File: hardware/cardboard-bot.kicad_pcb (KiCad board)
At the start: 2 copper layers, 80 x 46 mm, 101 parts, among them J1 USB-C CHARGE, J10 ESC PWR 2, J2 I2C, J3 MOTOR L, J4 MOTOR R, J5 OUT1, J6 OUT2, J7 IO3, J8 IO21, J9 ESC PWR 1, Q1 CJAC80N03 DSG, Q2 CJAC80N03 CHG, Q3 AGM30P05A, SW1 POWER, U1 BQ25887RGER, U2 HY2120-CB, U3 TPS563201DDCR, U4 XIAO ESP32-C3, U5 DRV8833PWPR, U6 74VHCT1G125

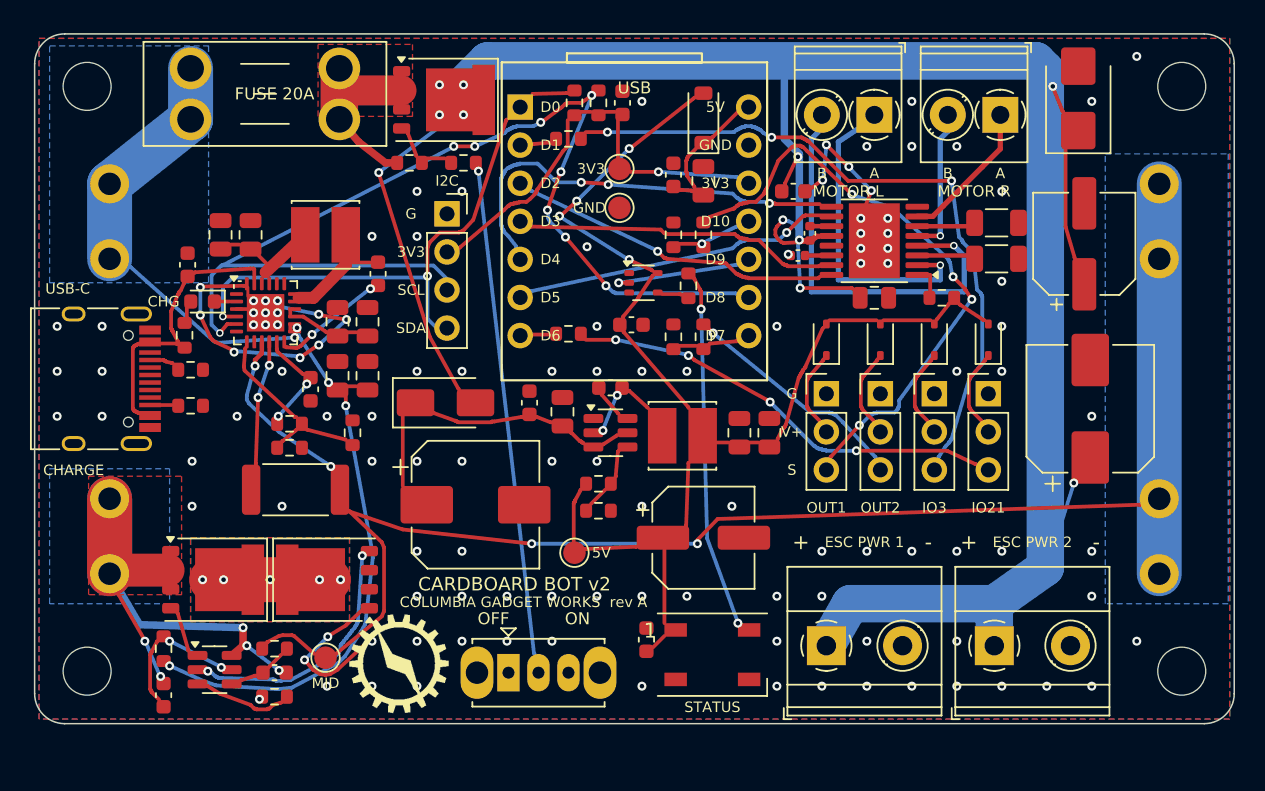
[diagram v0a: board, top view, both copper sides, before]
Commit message: Rework BOM for JLC stock: IP2320 charger, Basic parts, no shortfalls
Swap every out-of-stock or short part for a Basic, no-fee Preferred, or high-stock Extended part
(stock checked 28 Oct 2026):

- Charger: BQ25887 -> IP2320 (8.40 V / 1.0 A straps), plus 2x HY2213-BB3A cell balancers
  with AO3401A + 100R bleed
- Buck: TPS563201 (out of stock) -> TPS54202, same SOT-23-6 pinout, 75k/10k feedback
- Status LED: WS2812B-B (out of stock) -> XL-5050RGBC-2812B-S, run through a 1N4148W from 5 V;
  the 74VHCT1G125 level shifter is removed
- FETs: HYG015N03LS1C2 for the BMS, CJAB35P03 for the power switch
- Surge diode: SMAJ10A (Preferred)
- DRV8833 sense resistors: 0.1R Basic (2 A limit)
- Bulk electrolytics: through-hole, hand-soldered; the 220 uF on VSYS is dropped
- Battery sense: VSYS/4 on GPIO3 through cuttable jumper JP1

Re-placed and re-routed the charger and balancer area. DRC: no clearance errors,
no unconnected items; a new gnd_check.py confirms one GND cluster.
BOM: 35 lines, 12 Extended (was 18), about $6.40 of parts per board.
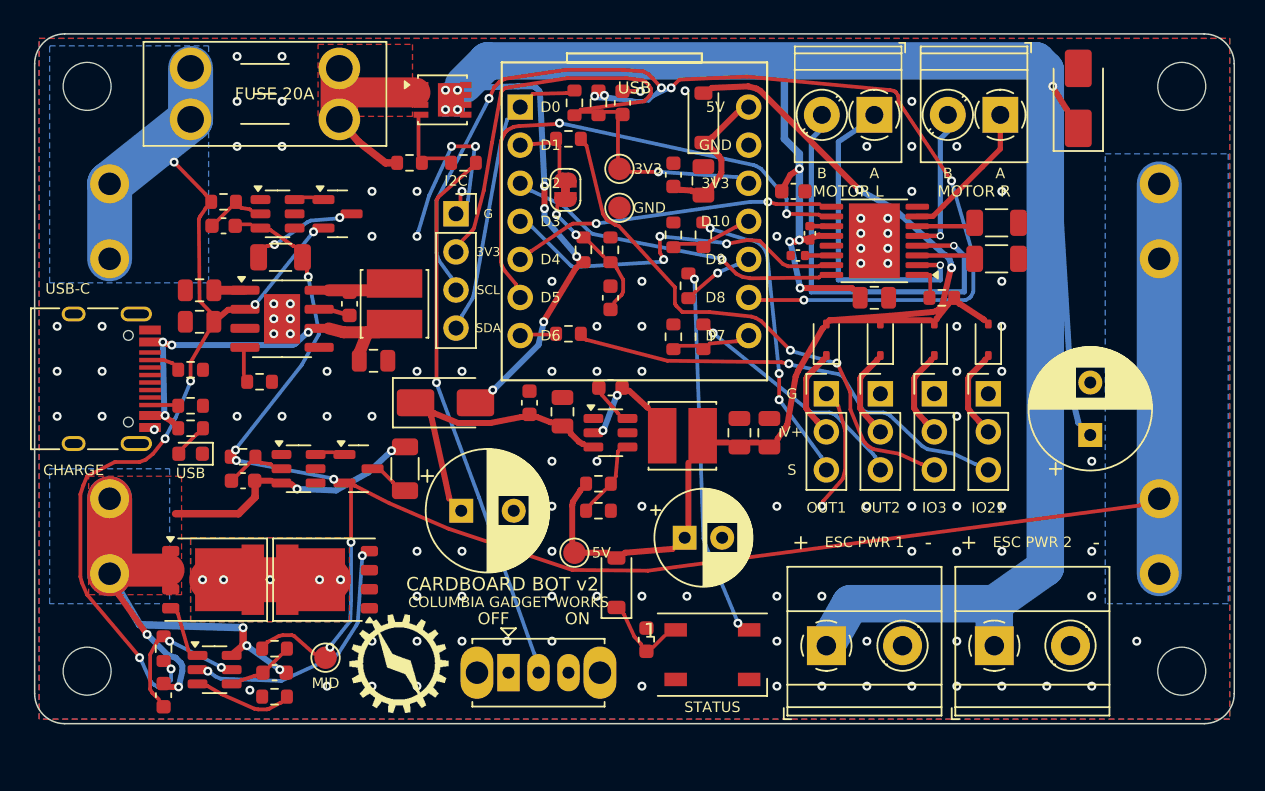
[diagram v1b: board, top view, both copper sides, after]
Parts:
- removed C12: 220uF 16V, Capacitor_SMD:CP_Elec_6.3x7.7
- removed C29: 100nF, Capacitor_SMD:C_0603_1608Metric
- removed C5: 4.7uF, Capacitor_SMD:C_0603_1608Metric
- removed C6, C7: 22uF, Capacitor_SMD:C_0805_2012Metric
- removed C8, C9: 10uF, Capacitor_SMD:C_0805_2012Metric
- removed R3: 22R 1W, Resistor_SMD:R_2512_6332Metric
- removed R5: 5.1k, Resistor_SMD:R_0603_1608Metric
- removed R6: 30k, Resistor_SMD:R_0603_1608Metric
- removed U6: 74VHCT1G125, Package_TO_SOT_SMD:SOT-353_SC-70-5
- added C31: 100nF, Capacitor_SMD:C_0603_1608Metric, F.Cu at (138.4, 117.6)
- added C32: 100nF, Capacitor_SMD:C_0603_1608Metric, F.Cu at (112.6, 112.8)
- added C33: 100nF, Capacitor_SMD:C_0603_1608Metric, F.Cu at (113.9, 129.8)
- added D10: 1N4148W, Diode_SMD:D_SOD-123, F.Cu at (138.8, 136.6)
- added JP1: VBAT>IO3, Jumper:SolderJumper-2_P1.3mm_Bridged_RoundedPad1.0x1.5mm, F.Cu at (135.4, 110.4)
- added Q4: AO3401A, Package_TO_SOT_SMD:SOT-23, F.Cu at (120.2, 112.0)
- added Q5: AO3401A, Package_TO_SOT_SMD:SOT-23, F.Cu at (121.6, 129.0)
- added R27: 300k, Resistor_SMD:R_0603_1608Metric, F.Cu at (136.6, 114.4)
- added R28: 100k, Resistor_SMD:R_0603_1608Metric, F.Cu at (138.4, 114.4)
- added R29: 330R, Resistor_SMD:R_0603_1608Metric, F.Cu at (112.6, 111.2)
- added R30: 100R, Resistor_SMD:R_1206_3216Metric, F.Cu at (116.4, 114.9)
- added R31: 330R, Resistor_SMD:R_0603_1608Metric, F.Cu at (113.9, 128.2)
- added R32: 100R, Resistor_SMD:R_1206_3216Metric, F.Cu at (124.7, 129.0)
- added U7: HY2213-BB3A, Package_TO_SOT_SMD:SOT-23-6, F.Cu at (116.2, 112.0)
- added U8: HY2213-BB3A, Package_TO_SOT_SMD:SOT-23-6, F.Cu at (117.6, 129.0)
- C1: value 1uF -> 22uF; footprint Capacitor_SMD:C_0603_1608Metric -> Capacitor_SMD:C_0805_2012Metric
- C13, C27: footprint Capacitor_SMD:CP_Elec_8x10 -> Capacitor_THT:CP_Radial_D8.0mm_P3.50mm
- C19: footprint Capacitor_SMD:CP_Elec_6.3x7.7 -> Capacitor_THT:CP_Radial_D6.3mm_P2.50mm
- C2: value 10uF -> 22uF
- C4: value 47nF -> 100nF
- D1: value YELLOW -> RED
- D2: value SMBJ9.0A -> SMAJ10A; footprint Diode_SMD:D_SMB -> Diode_SMD:D_SMA
- D9: value WS2812B -> XL-5050RGBC-2812B-S
- L1: value 1uH 4A -> 2.2uH 4.8A
- L2: value 4.7uH 2A -> 10uH 2.35A
- Q1: value CJAC80N03 DSG -> HYG015N03LS1C2 DSG
- Q2: value CJAC80N03 CHG -> HYG015N03LS1C2 CHG
- Q3: value AGM30P05A -> CJAB35P03; footprint Package_DFN_QFN:PQFN-8-EP_6x5mm_P1.27mm_Generic -> Package_SO:Vishay_PowerPAK_1212-8_Single
- R13: value 56k -> 75k
- R18, R19: value 0.15R -> 0.1R
- R7: value 2.2k -> 1k
- TH1: value 10k B3950 -> 10k B3380
- U1: value BQ25887RGER -> IP2320; footprint Package_DFN_QFN:VQFN-24-1EP_4x4mm_P0.5mm_EP2.5x2.5mm -> Package_SO:SOIC-8-1EP_3.9x4.9mm_P1.27mm_EP2.41x3.3mm
- U3: value TPS563201DDCR -> TPS54202DDCR
- moved C1 14.0 mm to (122.6, 121.8), turned to 0 degrees
- moved D1 10.2 mm to (110.4, 128.0)
- moved TH1 7.07 mm to (115.0, 123.2), turned to 0 degrees
- moved L1 6.51 mm to (124.0, 118.0), turned to 90 degrees
- moved R7 6.21 mm to (110.4, 126.3), turned to 0 degrees
- moved C3 5.97 mm to (111.0, 119.2), turned to 180 degrees
- moved C2 5.02 mm to (111.0, 117.1), turned to 180 degrees
- moved C4 2.76 mm to (121.0, 118.0)
- moved C27 1.75 mm to (170.4, 126.8)
- moved C19 1.25 mm to (143.3, 133.6)
- moved U1 1.17 mm to (116.5, 119.0)
- moved C13 1.03 mm to (128.4, 131.8)
- moved J2 0.60 mm to (128.1, 112.0)
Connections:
- net CHG_LED_A renamed PWR_LED_A
- C2 pad 1: PMID -> CHG_VSYS
- C3 pad 1: PMID -> BAT+
- C30 pad 1: +5V -> LED_VDD
- C4 pad 1: CHG_BTST -> CHG_BST
- C4 pad 2: CHG_SW -> CHG_LX
- D1 pad 1: CHG_STAT -> GND
- D9 pad 1: +5V -> LED_VDD
- L1 pad 1: PMID -> VBUS
- L1 pad 2: CHG_SW -> CHG_LX
- R26 pad 1: LED_DIN5 -> LED_DIN3
- TH1 pad 1: CHG_TS -> CHG_NTC
- U1 pad 1: (no net) -> CHG_VSYS
- U1 pad 2: CHG_STAT -> BAT+
- U1 pad 3: GND -> (no net)
- U1 pad 4: SDA -> CHG_NTC
- U1 pad 5: SCL -> (no net)
- U1 pad 6: (no net) -> VBUS
- U1 pad 7: CHG_TS -> CHG_BST
- U1 pad 8: GND -> CHG_LX
- U1 pad 9: MID -> GND
- U3 pad 5: VHOLD -> (no net)
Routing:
- net GND: track 44.1 -> 20.0 mm, vias 117 -> 114
- net OUT1_SIG: track 39.2 -> 19.0 mm, vias 4 -> 3
- net SDA: track 35.9 -> 15.9 mm, vias 2 -> 0
- net B_NEG: track 35.9 -> 53.6 mm, vias 5 -> 7
- net +3V3: track 23.0 -> 37.1 mm
- net BIN2: track 20.4 -> 34.0 mm, vias 1 -> 2
- net IO3_SIG: track 45.9 -> 34.7 mm, vias 3 -> 2
- net MID: track 106.7 -> 117.8 mm, vias 4 -> 6
- net CHG_TS: track 10.1 -> 0.00 mm
- net VSYS: track 163.1 -> 172.7 mm, vias 11 -> 14
- net CHG_CBSET: track 8.03 -> 0.00 mm, vias 2 -> 0
- net BIN1: track 27.6 -> 20.0 mm, vias 3 -> 2
- net CHG_SW: track 7.38 -> 0.00 mm
- net CHG_BTST: track 7.06 -> 0.00 mm, vias 2 -> 0
- net VBUS: track 15.1 -> 21.9 mm, vias 0 -> 4
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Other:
- board text added: "COLUMBIA GADGET WORKS"
- board text added: "USB"
- board text added: "github.com/ColumbiaGadgetWorks/cardboard-bot-v2 rev A"
- board text removed: "CHG"
- board text removed: "COLUMBIA GADGET WORKS rev A"
- board text removed: "github.com/ColumbiaGadgetWorks/cardboard-bot-v2"

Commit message: Rev A: apply datasheet checks, re-layout around real 18650 clip footprint
- MY-18650-01 clip footprint per drawing (3 legs, 1.8 mm holes, 48 mm per cell);
  cells, BMS, balancers and charger re-placed, board re-routed, DRC clean
- IP2320 wired per typical application: VIN RC + 5.1k, VSET/NTC caps,
  charge LED on LED/ISET
- HY2213 VDD resistor 100R
- Regenerated gerbers, BOM, CPL, BOM check and previews
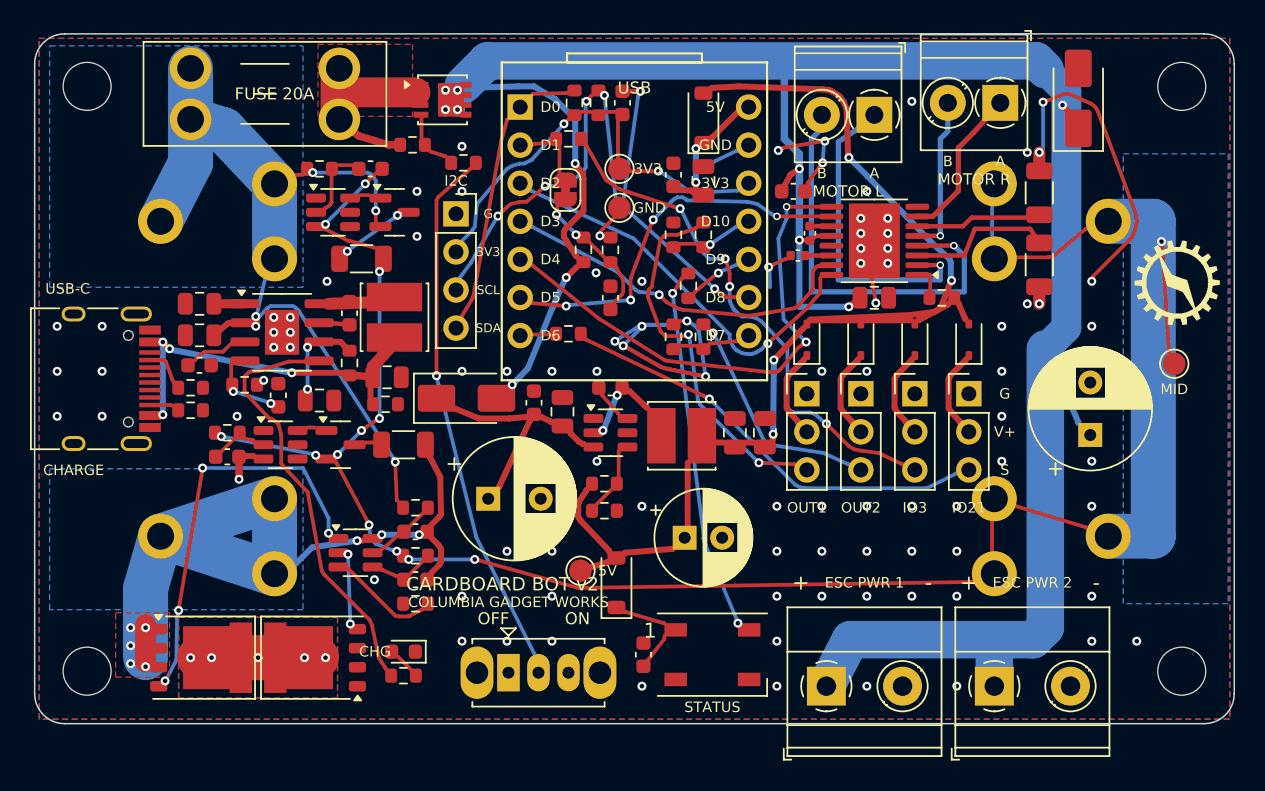
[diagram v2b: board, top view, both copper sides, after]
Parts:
- added C5: 10uF, Capacitor_SMD:C_0805_2012Metric, F.Cu at (119.0, 124.5)
- added C6: 100nF, Capacitor_SMD:C_0603_1608Metric, F.Cu at (111.0, 122.1)
- added C7: 100nF, Capacitor_SMD:C_0603_1608Metric, F.Cu at (116.2, 124.1)
- added R3: 5.1k, Resistor_SMD:R_0603_1608Metric, F.Cu at (123.4, 124.7)
- added R4: 1R, Resistor_SMD:R_0603_1608Metric, F.Cu at (121.0, 122.0)
- LOGO1: value CGW_Logo_7mm -> CGW_Logo_6mm; footprint cgw:CGW_Logo_7mm -> cgw:CGW_Logo_6mm
- R29, R31: value 330R -> 100R
- U1: footprint Package_SO:SOIC-8-1EP_3.9x4.9mm_P1.27mm_EP2.41x3.3mm -> Package_SO:SOIC-8-1EP_3.9x4.9mm_P1.27mm_EP2.29x3mm
- moved TP7 59.9 mm to (176.0, 122.0)
- moved LOGO1 57.8 mm to (176.2, 116.6)
- moved R7 21.8 mm to (124.6, 142.8)
- moved C10 20.0 mm to (125.4, 133.2), turned to 0 degrees
- moved D1 19.4 mm to (124.6, 141.2)
- moved R8 19.3 mm to (125.4, 131.6), turned to 0 degrees
- moved U2 12.2 mm to (121.4, 134.6)
- moved C11 11.3 mm to (125.4, 136.4)
- moved R10 11.3 mm to (125.4, 138.0)
- moved R9 11.3 mm to (125.4, 134.8)
- moved BT1 11.0 mm to (116.0, 133.5)
- moved BT2 11.0 mm to (164.0, 112.5), turned to 180 degrees
- moved BT3 11.0 mm to (164.0, 133.5), turned to 180 degrees
- moved BT4 11.0 mm to (116.0, 112.5)
- moved C32 10.5 mm to (122.4, 109.0)
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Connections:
- net PWR_LED_A renamed CHG_LED_A
- R7 pad 1: VBUS -> CHG_LED
- U1 pad 3: (no net) -> CHG_VSET
- U1 pad 5: (no net) -> CHG_LED
- U1 pad 6: VBUS -> CHG_VIN
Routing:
- net GND: track 20.0 -> 70.2 mm, vias 114 -> 97
- net SCL: track 79.8 -> 34.3 mm, vias 7 -> 5
- net CHG_LED: track 0.00 -> 27.0 mm
- net BMS_DO: track 2.67 -> 26.1 mm, vias 0 -> 4
- net +3V3: track 37.1 -> 22.6 mm, vias 1 -> 2
- net BIN1: track 20.0 -> 33.9 mm
- net BAT+: track 67.3 -> 53.9 mm, vias 7 -> 5
- net VSYS: track 172.7 -> 160.1 mm, vias 14 -> 11
- net BMS_CO: track 16.2 -> 4.65 mm
- net BIN2: track 34.0 -> 24.9 mm, vias 2 -> 4
- net DRV_AISEN: track 3.92 -> 9.87 mm
- net BMS_VDD: track 8.12 -> 2.57 mm, vias 2 -> 0
- net AIN1: track 20.9 -> 26.1 mm
- net MID: track 117.8 -> 122.8 mm, vias 6 -> 13
- net OUT1_SIG: track 19.0 -> 23.8 mm, vias 3 -> 2
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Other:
- board text added: "CHG"
- board text removed: "USB"
